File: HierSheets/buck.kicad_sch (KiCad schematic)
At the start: 0 parts

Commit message: .
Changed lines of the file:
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@@
 		)
 	)
-	(hierarchical_label "12V"
-		(shape passive)
+	(hierarchical_label "IN12V"
+		(shape input)
 		(at 195.58 123.19 0)
 		(effects
@@
 		)
 	)
-	(hierarchical_label "5V"
-		(shape passive)
+	(hierarchical_label "OUT5V"
+		(shape output)
 		(at 118.11 123.19 180)
 		(effects

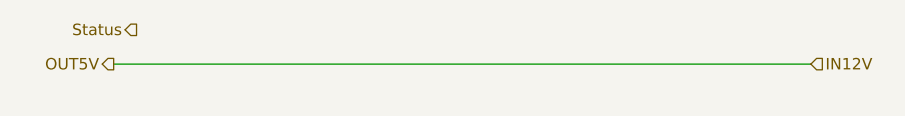
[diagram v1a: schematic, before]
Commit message: Added Libs folder and lib for eFuse
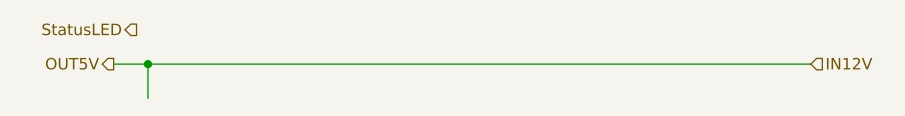
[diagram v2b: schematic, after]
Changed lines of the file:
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@@
 	(generator_version "10.0")
 	(paper "A4")
+	(junction
+		(at 121.92 123.19)
+		(diameter 0)
+		(color 0 0 0 0)
+	)
 	(wire
 		(pts
-			(xy 118.11 123.19) (xy 195.58 123.19)
+			(xy 121.92 123.19) (xy 121.92 127)
+		)
+		(stroke
+			(width 0)
+			(type default)
+		)
+	)
+	(wire
+		(pts
+			(xy 121.92 123.19) (xy 195.58 123.19)
+		)
+		(stroke
+			(width 0)
+			(type default)
+		)
+	)
+	(wire
+		(pts
+			(xy 118.11 123.19) (xy 121.92 123.19)
 		)
 		(stroke
@@
 		)
 	)
-	(hierarchical_label "Status"
+	(hierarchical_label "StatusLED"
 		(shape output)
 		(at 120.65 119.38 180)

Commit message: Efuse added, not set.
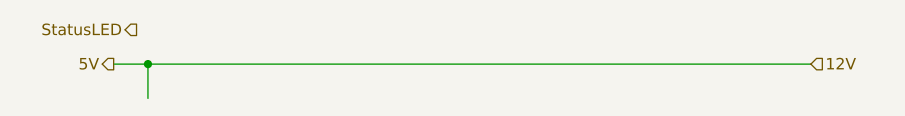
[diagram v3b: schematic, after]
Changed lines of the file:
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@@
 		)
 	)
-	(hierarchical_label "IN12V"
+	(hierarchical_label "12V"
 		(shape input)
 		(at 195.58 123.19 0)
@@
 		)
 	)
-	(hierarchical_label "OUT5V"
+	(hierarchical_label "5V"
 		(shape output)
 		(at 118.11 123.19 180)

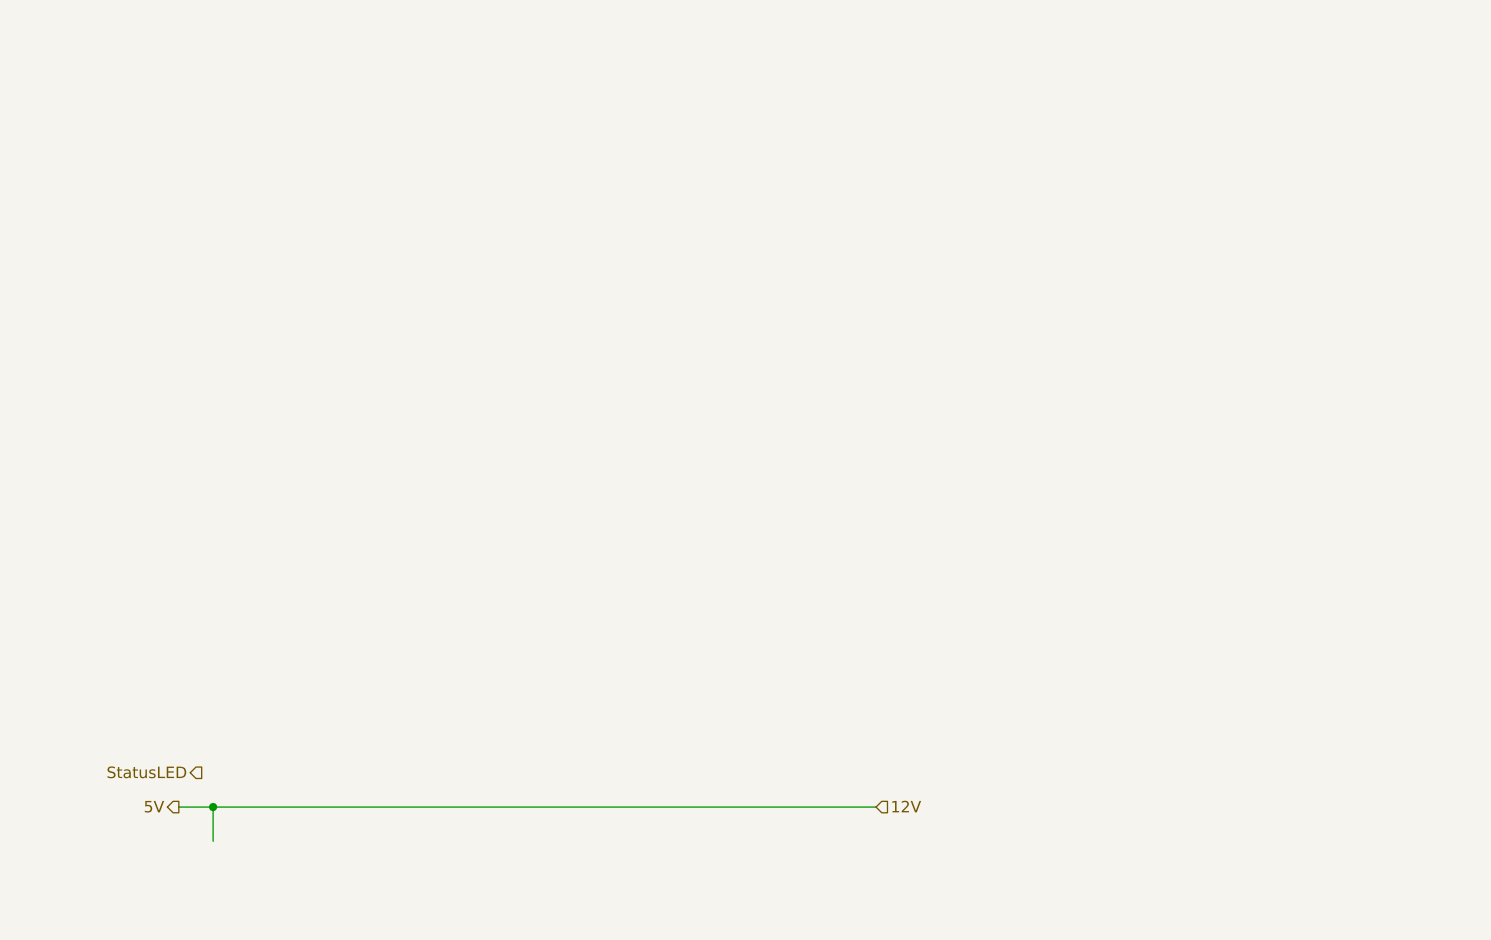
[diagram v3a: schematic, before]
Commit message: Added kicker, interrupt, I2C pullups, buck converter, button
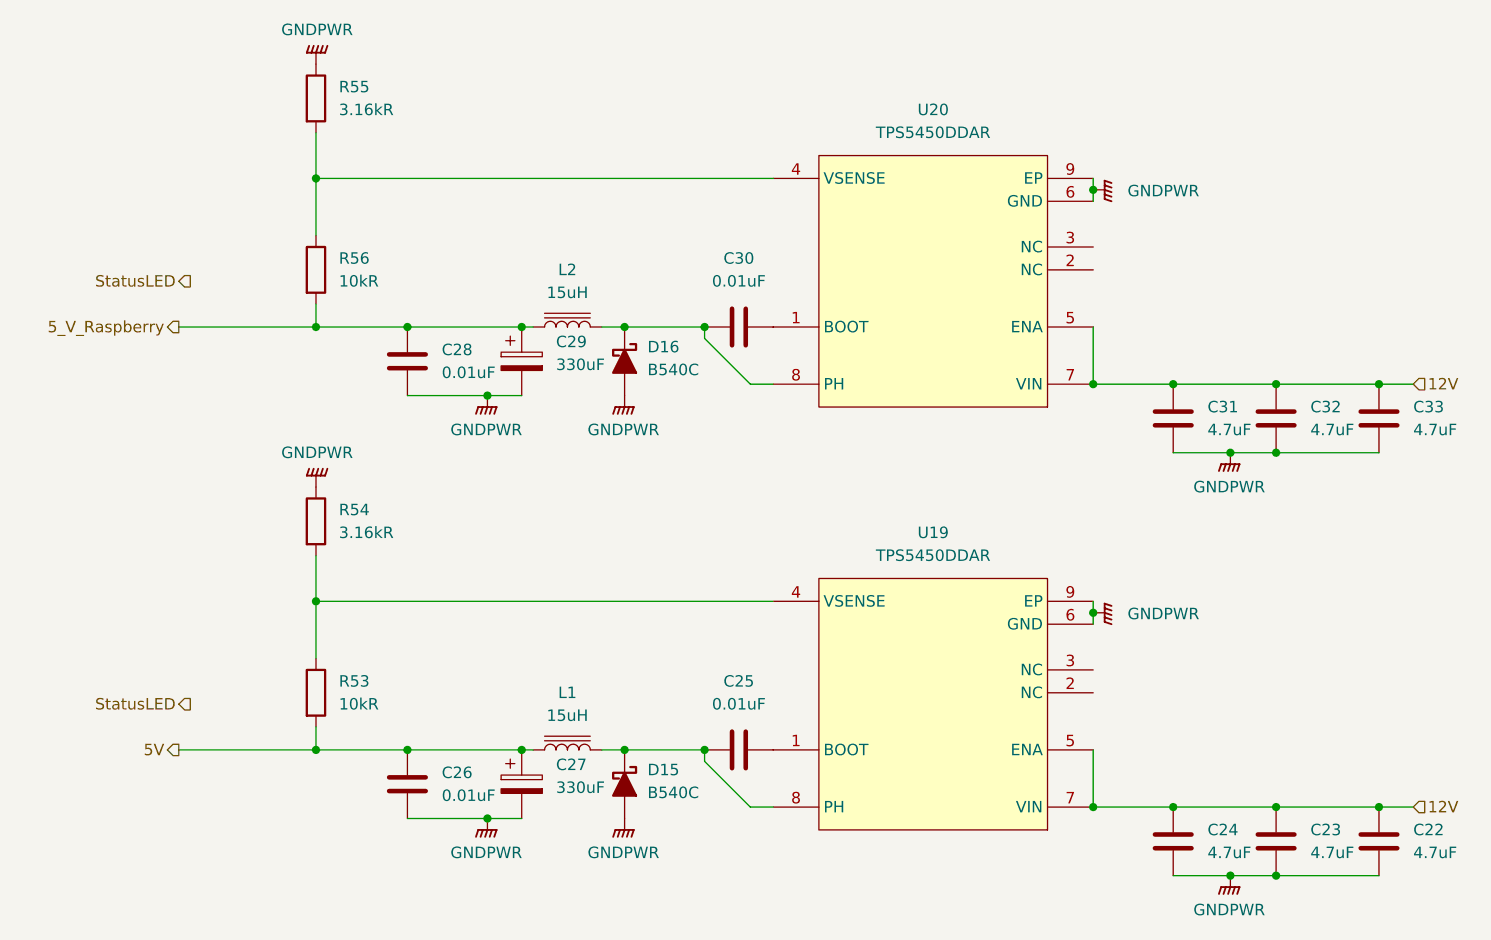
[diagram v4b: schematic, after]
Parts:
- added C22, C23, C24, C31, C32, C33: 4.7uF, symbol Device:C
- added C25, C26, C28, C30: 0.01uF, symbol Device:C
- added C27, C29: 330uF, symbol Device:C_Polarized
- added D15, D16: B540C, symbol Device:D_Schottky_Filled
- added L1, L2: 15uH, symbol Device:L_Iron
- added R53, R56: 10kR, symbol Device:R
- added R54, R55: 3.16kR, symbol Device:R
- added U19, U20: TPS5450DDAR, easyeda2kicad:SOP-8_L4.9-W3.9-P1.27-LS6.0-BL-EP, symbol EasyEDA2Kicad:TPS5450DDAR
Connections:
- net 12V: now also C22.2, C23.2, C24.2, C31.2, C32.2, C33.2, U19.5 (ENA), U19.7 (VIN), U20.5 (ENA), U20.7 (VIN)
- new net: C25.1, D15.1 (K), L1.2, U19.8 (PH)
- new net: C25.2, U19.1 (BOOT)
- new net: C30.1, D16.1 (K), L2.2, U20.8 (PH)
- new net: C30.2, U20.1 (BOOT)
- new net: R53.1, R54.2, U19.4 (VSENSE)
- new net: R55.2, R56.1, U20.4 (VSENSE)
- new net 5V: C26.2, C27.1, L1.1, R53.2
- new net 5_V_Raspberry: C28.2, C29.1, L2.1, R56.2
- new net GNDPWR: C22.1, C23.1, C24.1, C26.1, C27.2, C28.1, C29.2, C31.1, C32.1, C33.1, D15.2 (A), D16.2 (A), R54.1, R55.1, U19.6 (GND), U19.9 (EP), U20.6 (GND), U20.9 (EP)
